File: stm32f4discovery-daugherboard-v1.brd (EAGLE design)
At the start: 100 x 71.1 mm, 41 parts

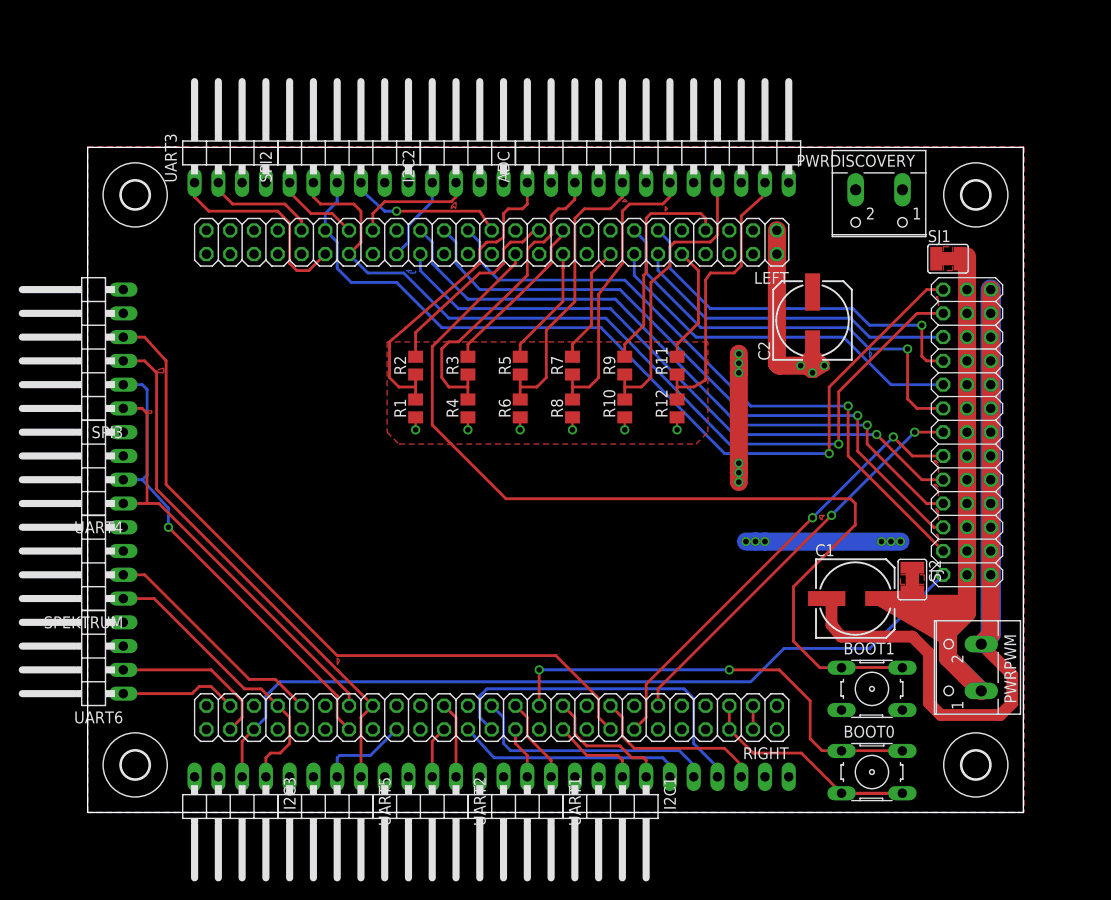
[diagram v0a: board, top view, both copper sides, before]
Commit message: replaced v1 with v2
deleted v1, renamed v2 to v1
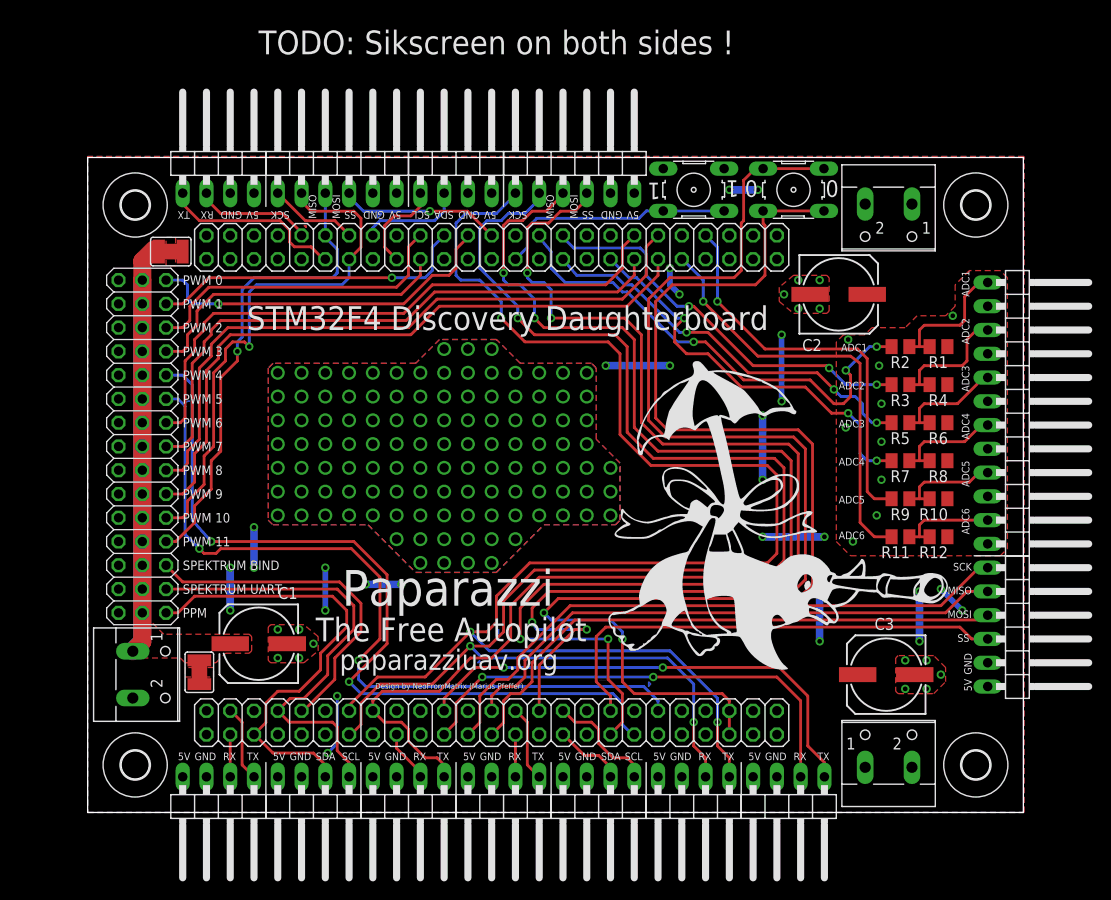
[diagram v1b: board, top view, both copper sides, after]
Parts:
- removed SPEKTRUM: 1x4, pinhead:1X04/90
- added C3: (no value), rcl:153CLV-0807
- added PWRDISCOVERY1: screw terminal, con-wago-500:W237-102
- added U$2, U$3: PAPARAZZI, paparazzi:PAPARAZZI
- U$1: value 3X13 -> 3X15; device pinhead3:3X13 -> pinhead3:3X15
- moved SJ1 91.4 mm to (11.9, 15.0), turned to 90 degrees
- moved U$1 89.2 mm to (5.84, 39.1), turned to 270 degrees
- moved PWRPWM 88.1 mm to (6.10, 14.7), turned to 270 degrees
- moved SJ2 86.7 mm to (8.89, 59.9), turned to 180 degrees
- moved UART4 74.5 mm to (64.8, 0.00), turned to 180 degrees
- moved C1 63.9 mm to (18.3, 18.0), turned to 180 degrees
- moved BOOT0 62.8 mm to (75.4, 66.5)
- moved BOOT1 56.6 mm to (64.8, 66.5), turned to 180 degrees
- moved R1 56.3 mm to (90.9, 49.8), turned to 180 degrees
- moved SPI3 55.9 mm to (52.1, 70.0), turned to 0 degrees
- moved R2 51.9 mm to (86.9, 49.8), turned to 180 degrees
- moved R4 50.4 mm to (90.9, 45.7), turned to 180 degrees
- moved ADC 48.3 mm to (100.0, 42.7), turned to 270 degrees
- moved R3 46.3 mm to (86.9, 45.7), turned to 180 degrees
- moved R6 44.7 mm to (90.9, 41.7), turned to 180 degrees
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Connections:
- net GND: now also C3.-, PWRDISCOVERY1.2, U$1.GND14, U$1.GND15; no longer SPEKTRUM.4
- net PA0: now also U$1.SIG10; no longer U$1.SIG11
- net PA1: now also U$1.SIG9; no longer U$1.SIG10
- net PA10: now also U$1.SIG13; no longer SPEKTRUM.2
- net PA2: now also U$1.SIG8; no longer U$1.SIG9
- net PA3: now also U$1.SIG7; no longer U$1.SIG8
- net PA8: now also U$1.SIG14; no longer SPEKTRUM.1
- net PB14: now also U$1.SIG11; no longer U$1.SIG12
- net PB15: now also U$1.SIG12; no longer U$1.SIG13
- net PC9: now also U$1.SIG15; no longer U$1.SIG1
- net PE11: now also U$1.SIG2; no longer U$1.SIG3
- net PE13: now also U$1.SIG3; no longer U$1.SIG4
- net PE14: now also U$1.SIG4; no longer U$1.SIG5
- net PE5: now also U$1.SIG5; no longer U$1.SIG6
- net PE6: now also U$1.SIG6; no longer U$1.SIG7
- net PE9: now also U$1.SIG1; no longer U$1.SIG2
- net PWM_VIN: now also U$1.PWR14, U$1.PWR15
- net VIN: now also C3.+, PWRDISCOVERY1.1; no longer SPEKTRUM.3
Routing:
- net GND: track 150.7 -> 0.00 mm, vias 15 -> 24
- net PC10: track 46.2 -> 163.9 mm, vias 0 -> 3
- net PC11: track 50.4 -> 163.4 mm, vias 1 -> 3
- net 3V: track 23.9 -> 132.1 mm, vias 0 -> 2
- net PC12: track 57.4 -> 136.4 mm, vias 0 -> 2
- net BOOT0: track 48.7 -> 124.8 mm
- net PB2: track 94.4 -> 25.7 mm
- net VIN: track 16.5 -> 71.1 mm, vias 6 -> 28
- net PWM_VIN: track 134.8 -> 84.0 mm
- net PE3: track 78.5 -> 125.9 mm, vias 0 -> 4
- net PD6: track 5.60 -> 51.0 mm, vias 0 -> 2
- net PD5: track 8.14 -> 52.2 mm, vias 0 -> 2
- net PB15: track 94.7 -> 50.8 mm
- net PE6: track 43.6 -> 85.1 mm
- net PB3: track 24.5 -> 65.3 mm
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- added copper zone on layer 1, net GND
- added copper zone on layer 1, net N$12
- added copper zone on layer 1, net N$120
- added copper zone on layer 16, net N$121
- added copper zone on layer 16, net N$17
- added copper zone on layer 16, net N$18
- added copper zone on layer 16, net N$19
- added copper zone on layer 1, net N$2
- added copper zone on layer 16, net N$20
- added copper zone on layer 16, net N$21
- added copper zone on layer 1, net PWM_VIN
- removed copper zone on layer 16, net N$12
- removed copper zone on layer 1, net N$13
- removed copper zone on layer 1, net N$14
- removed copper zone on layer 16, net N$16
- removed copper zone on layer 1, net N$17
- removed copper zone on layer 1, net N$19
- removed copper zone on layer 1, net N$20
- removed copper zone on layer 1, net N$21
- removed copper zone on layer 1, net N$22
- removed copper zone on layer 1, net N$23
- removed copper zone on layer 1, net N$24
- removed copper zone on layer 1, net N$25
- removed copper zone on layer 1, net N$26
- removed copper zone on layer 1, net N$27
- removed copper zone on layer 1, net N$6
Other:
- board size 100 x 71.1 mm -> 100 x 70 mm
- board text added: "0"
- board text added: "1"
- board text added: "5V"
- board text added: "ADC 1"
- board text added: "ADC 2"
- board text added: "ADC 3"
- board text added: "ADC 4"
- board text added: "ADC 5"
- board text added: "ADC 6"
- board text added: "ADC1"
- board text added: "ADC2"
- board text added: "ADC3"
- board text added: "ADC4"
- board text added: "ADC5"
- board text added: "ADC6"
- board text added: "Design by NeoFromMatrix (Marius Pfeffer)"
- board text added: "GND"
- board text added: "MISO"
- board text added: "MOSI"
- board text added: "PPM"
- board text added: "PPM IN"
- board text added: "PWM 0"
- board text added: "PWM 1"
- board text added: "PWM 10"
- board text added: "PWM 11"
- board text added: "PWM 2"
- board text added: "PWM 3"
- board text added: "PWM 4"
- board text added: "PWM 5"
- board text added: "PWM 6"
- board text added: "PWM 7"
- board text added: "PWM 8"
- board text added: "PWM 9"
- board text added: "PWM VIN"
- board text added: "Paparazzi"
- board text added: "RX"
- board text added: "SCK"
- board text added: "SCL"
- board text added: "SDA"
- board text added: "SPEKTRUM BIND"
- board text added: "SPEKTRUM UART"
- board text added: "SS"
- board text added: "STM32F4 Discovery Daughterboard"
- board text added: "TODO: Sikscreen on both sides !"
- board text added: "TX"
- board text added: "The Free Autopilot"
- board text added: "VIN"
- board text added: "paparazziuav.org"

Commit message: small changes
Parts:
- moved U$3 1.83 mm to (53.6, 12.7)
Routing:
- net PC12: track 136.4 -> 135.1 mm
- net PE3: track 125.9 -> 125.1 mm
- net BOOT0: track 124.8 -> 124.2 mm
- net 3V: track 132.1 -> 131.5 mm
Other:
- board text added: "PWR"
- board text added: "SIGNAL"
- board text added: "SPEK BIND"
- board text added: "SPEK UART"
